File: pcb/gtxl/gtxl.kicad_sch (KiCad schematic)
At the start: 0 parts

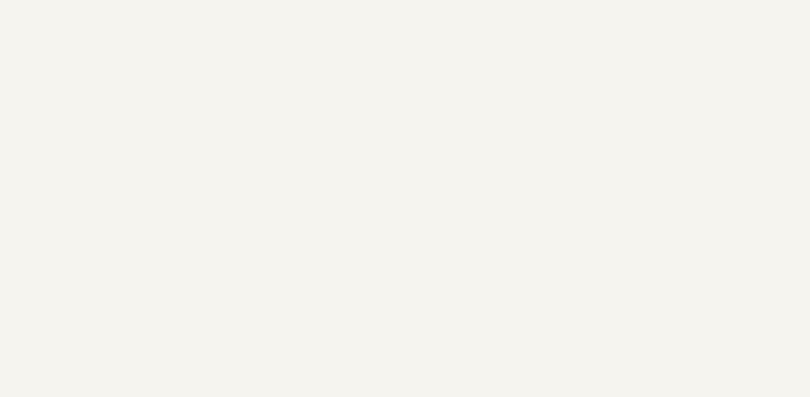
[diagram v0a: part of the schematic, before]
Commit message: Update schematic with removed timer.  Update video timing notes.
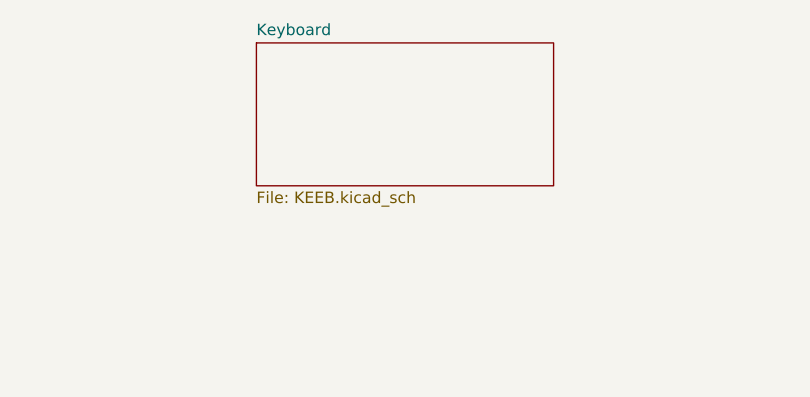
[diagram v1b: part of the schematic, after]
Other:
- added sheet Keyboard (KEEB.kicad_sch)
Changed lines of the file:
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@@
 	(paper "B")
+	(sheet
+		(at 95.885 90.805)
+		(size 33.02 15.875)
+		(fields_autoplaced yes)
+		(stroke
+			(width 0.1524)
+			(type solid)
+		)
+		(fill
+			(color 0 0 0 0.0000)
+		)
+		(property "Sheetname" "Keyboard"
+			(at 95.885 90.0934 0)
+			(effects
+				(font
+					(size 1.27 1.27)
+				)
+				(justify left bottom)
+			)
+		)
+		(property "Sheetfile" "KEEB.kicad_sch"
+			(at 95.885 107.2646 0)
+			(effects
+				(font
+					(size 1.27 1.27)
+				)
+				(justify left top)
+			)
+		)
+		(instances
+			(project "gtxl"
+				(path "/2dd80149-0e94-4467-bb5a-52cd819c450a"
+					(page "9")
+				)
+			)
+		)
+	)
 	(sheet
 		(at 116.205 137.795)
@@
 			(project "gtxl"
 				(path "/2dd80149-0e94-4467-bb5a-52cd819c450a"
-					(page "3")
+					(page "4")
 				)
 			)
@@
 			(project "gtxl"
 				(path "/2dd80149-0e94-4467-bb5a-52cd819c450a"
-					(page "4")
+					(page "2")
 				)
 			)
@@
 			(project "gtxl"
 				(path "/2dd80149-0e94-4467-bb5a-52cd819c450a"
-					(page "2")
-				)
-			)
+					(page "3")
+				)
+			)
